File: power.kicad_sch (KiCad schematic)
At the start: 33 parts, among them J1 POWER, Q5 2N3906, Q6 2N3904, Q7 2N3904, U1 TL072, U2 TL072, U3 LM7812_TO220, U3 NE555P, U4 LM7805_TO220, U9 LM358

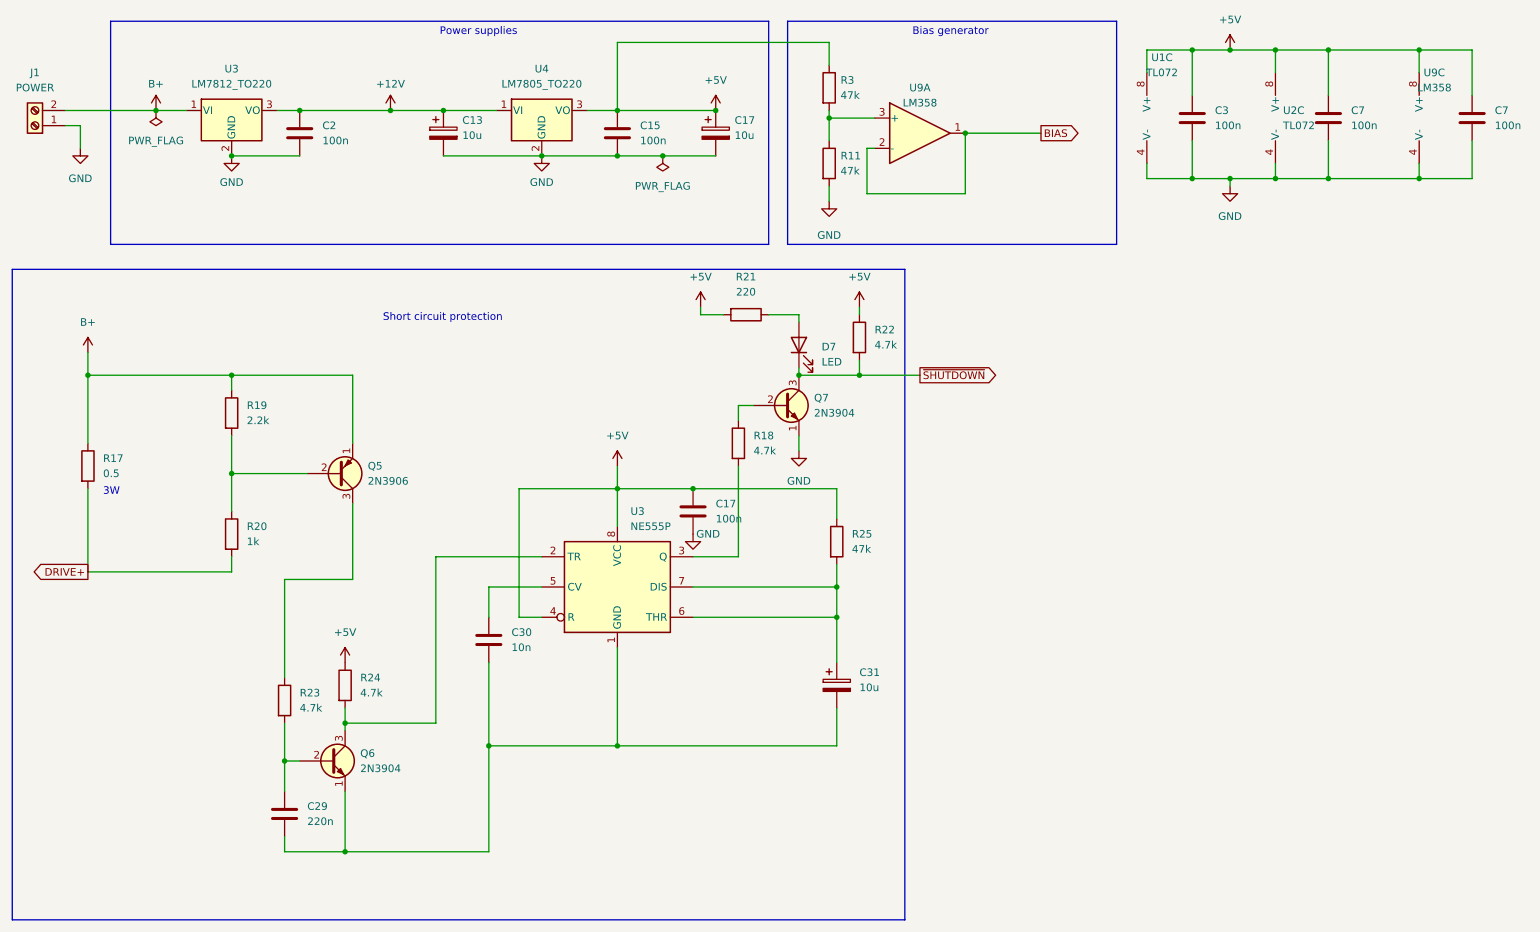
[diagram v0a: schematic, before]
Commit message: Added right channel
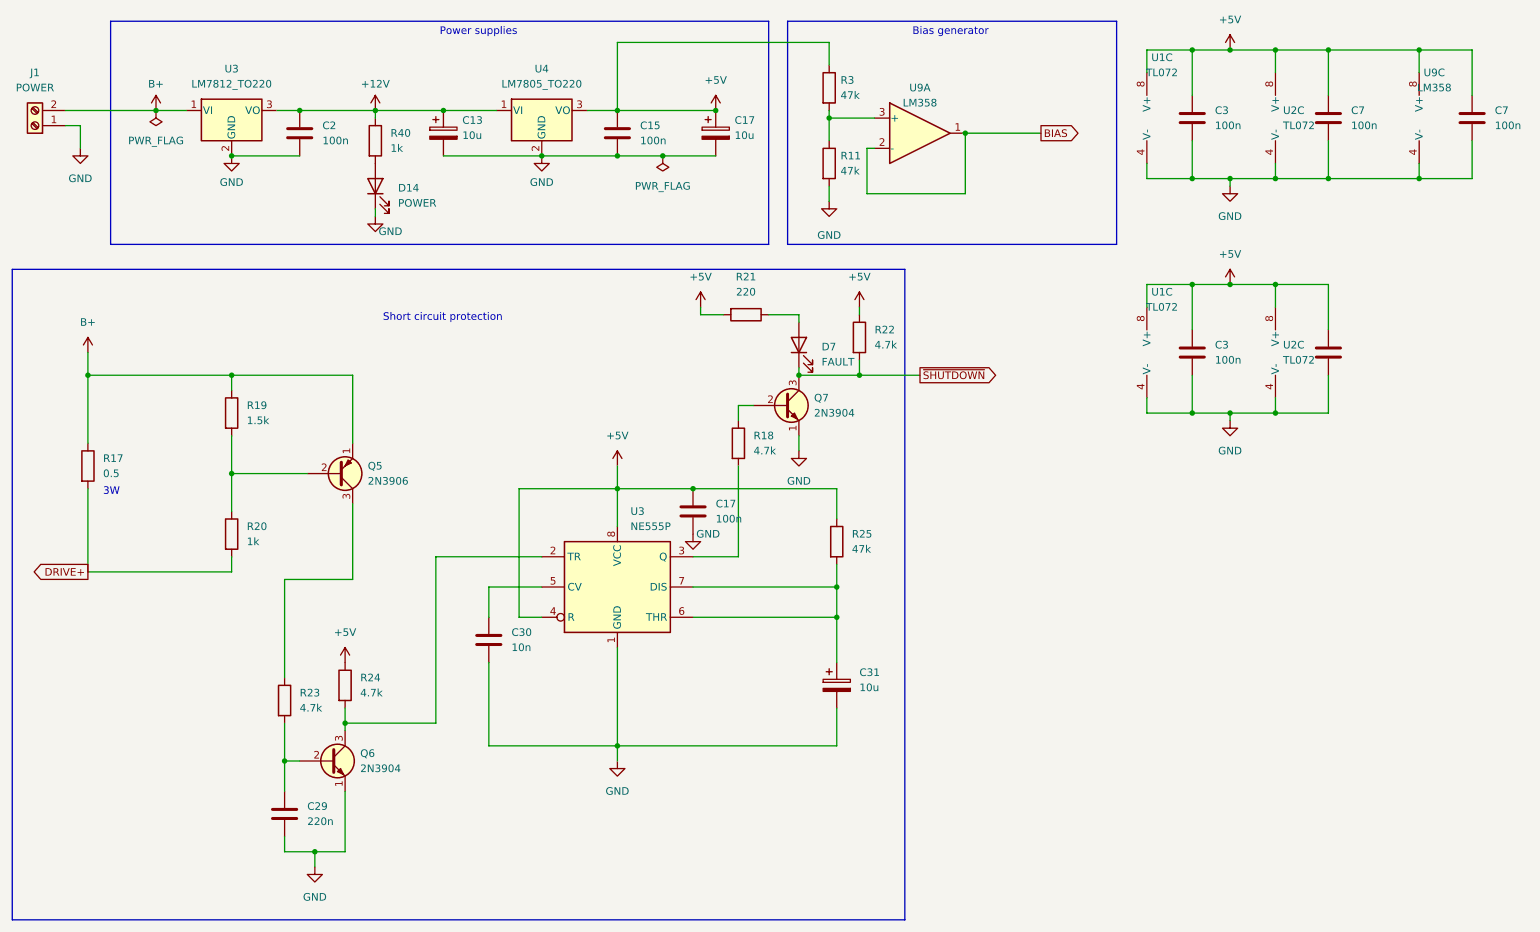
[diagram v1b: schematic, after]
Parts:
- added C3, C7: 100n, Capacitor_THT:C_Disc_D3.4mm_W2.1mm_P2.50mm, symbol Device:C
- added D14: POWER, LED_THT:LED_D4.0mm, symbol Device:LED
- added R40: 1k, Resistor_THT:R_Axial_DIN0204_L3.6mm_D1.6mm_P7.62mm_Horizontal, symbol Device:R
- added U1, U2: TL072, PCM_Package_DIP_AKL:DIP-8_W7.62mm, symbol Amplifier_Operational:TL072
- D7: value LED -> FAULT; footprint Diode_THT:D_DO-41_SOD81_P10.16mm_Horizontal -> LED_THT:LED_D4.0mm
- R19: value 2.2k -> 1.5k
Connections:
- net +12V: now also R40.1
- net +5V: now also C3.1, C7.1, U1.8 (V+), U2.8 (V+)
- net GND: now also C29.2, C30.2, C31.2, Q6.1 (E), U3.1 (GND), C3.2, C7.2, D14.1 (K), U1.4 (V-), U2.4 (V-)
- new net: D14.2 (A), R40.2

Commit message: Pre layer elimination
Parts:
- R22: value 4.7k -> 3.9k
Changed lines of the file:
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@@
       (effects (font (size 1.27 1.27)) (justify left))
     )
-    (property "Value" "4.7k" (at 170.18 81.28 0)
+    (property "Value" "3.9k" (at 170.18 81.28 0)
       (effects (font (size 1.27 1.27)) (justify left))
     )

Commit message: WIP
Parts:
- added J5: POWER, TerminalBlock_4Ucon:TerminalBlock_4Ucon_1x02_P3.50mm_Horizontal, symbol Connector:Screw_Terminal_01x02
- added Q12: 2N3906, Package_TO_SOT_THT:TO-92_Inline, symbol PCM_Transistor_BJT_AKL:2N3906
- added R43, R45: 1k, Resistor_THT:R_Axial_DIN0204_L3.6mm_D1.6mm_P7.62mm_Horizontal, symbol Device:R
- added R44: 1.5k, Resistor_THT:R_Axial_DIN0204_L3.6mm_D1.6mm_P7.62mm_Horizontal, symbol Device:R
- added R46: 4.7k, Resistor_THT:R_Axial_DIN0204_L3.6mm_D1.6mm_P7.62mm_Horizontal, symbol Device:R
- added R47: 0.5, Resistor_THT:R_Axial_DIN0922_L20.0mm_D9.0mm_P25.40mm_Horizontal, symbol Device:R
- C29: value 220n -> 10u; footprint Capacitor_THT:C_Disc_D3.4mm_W2.1mm_P2.50mm -> Capacitor_THT:CP_Radial_D4.0mm_P1.50mm; symbol Device:C -> Device:C_Polarized
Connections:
- net GND: now also J5.1 (Pin_1), R43.2
- net at C29.1, Q6.2 (B), R23.2: now also R43.1, R46.2
- net B+ renamed LPWR+
- net DRIVE+ renamed LDRIVE+
- new net: Q12.3 (C), R46.1
- new net: Q12.2 (B), R44.2, R45.1
- new net RDRIVE+: R45.2, R47.2
- new net RPWR+: J5.2 (Pin_2), Q12.1 (E), R44.1, R47.1
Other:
- moved on the sheet: Q5, Q6, R19, R20, R23, R24

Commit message: Ver 1.1
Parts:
- added unit 2 of U9
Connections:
- net GND: now also U9.5 (+)
- new net: U9.6 (-), U9.7
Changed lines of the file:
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@@
+    (stroke (width 0) (type default))
+  )
+  (wire (pts (xy 212.09 134.62) (xy 212.09 140.335))
     (stroke (width 0) (type default))
   )
@@
     (stroke (width 0) (type default))
   )
+  (wire (pts (xy 247.65 137.16) (xy 242.57 137.16))
+    (stroke (width 0) (type default))
+  )
   (wire (pts (xy 229.87 53.34) (xy 237.49 53.34))
     (stroke (width 0) (type default))
@@
     (stroke (width 0) (type default))
   )
+  (wire (pts (xy 222.885 147.32) (xy 247.65 147.32))
+    (stroke (width 0) (type default))
+  )
   (wire (pts (xy 83.82 86.36) (xy 83.82 88.9))
     (stroke (width 0) (type default))
@@
     (stroke (width 0) (type default))
   )
+  (wire (pts (xy 222.885 139.7) (xy 222.885 147.32))
+    (stroke (width 0) (type default))
+  )
   (wire (pts (xy 76.2 107.95) (xy 76.2 137.16))
     (stroke (width 0) (type default))
@@
     (stroke (width 0) (type default))
   )
+  (wire (pts (xy 227.33 134.62) (xy 212.09 134.62))
+    (stroke (width 0) (type default))
+  )
   (wire (pts (xy 223.52 71.12) (xy 229.87 71.12))
     (stroke (width 0) (type default))
@@
     (stroke (width 0) (type default))
   )
+  (wire (pts (xy 227.33 139.7) (xy 222.885 139.7))
+    (stroke (width 0) (type default))
+  )
   (wire (pts (xy 76.2 86.36) (xy 76.2 97.79))
     (stroke (width 0) (type default))
@@
   )
   (wire (pts (xy 127 148.59) (xy 163.83 148.59))
+    (stroke (width 0) (type default))
+  )
+  (wire (pts (xy 247.65 147.32) (xy 247.65 137.16))
     (stroke (width 0) (type default))
   )
@@
     (property "Intersheetrefs" "${INTERSHEET_REFS}" (at 70.07 115.57 0)
       (effects (font (size 1.27 1.27)) (justify right) hide)
+    )
+  )
+  (symbol (lib_id "power:GND") (at 212.09 140.335 0) (unit 1)
+    (in_bom yes) (on_board yes) (dnp no) (fields_autoplaced)
+    (property "Reference" "#PWR067" (at 212.09 146.685 0)
+      (effects (font (size 1.27 1.27)) hide)
+    )
+    (property "Value" "GND" (at 212.09 144.78 0)
+      (effects (font (size 1.27 1.27)))
+    )
+    (property "Footprint" "" (at 212.09 140.335 0)
+      (effects (font (size 1.27 1.27)) hide)
+    )
+    (property "Datasheet" "" (at 212.09 140.335 0)
+      (effects (font (size 1.27 1.27)) hide)
+    )
+    (pin "1")
+    (instances
+      (project "classd-amp"
+        (path "/4342a3a3-4383-4661-90ac-821979f46c8c/3b3caeaf-3878-4281-86ae-73a7190e5fd4"
+          (reference "#PWR067") (unit 1)
+        )
+      )
     )
   )
@@
         )
       )
+    )
+  )
+  (symbol (lib_id "Amplifier_Operational:LM358") (at 234.95 137.16 0) (unit 2)
+    (in_bom yes) (on_board yes) (dnp no)
+    (property "Reference" "U9" (at 234.95 129.54 0)
+      (effects (font (size 1.27 1.27)))
+    )
+    (property "Value" "LM358" (at 234.95 132.08 0)
+      (effects (font (size 1.27 1.27)))
+    )
+    (property "Footprint" "PCM_Package_DIP_AKL:DIP-8_W7.62mm" (at 234.95 137.16 0)
+      (effects (font (size 1.27 1.27)) hide)
+    )
+    (property "Datasheet" "http://www.ti.com/lit/ds/symlink/lm2904-n.pdf" (at 234.95 137.16 0)
+      (effects (font (size 1.27 1.27)) hide)
+    )
+    (property "Sim.Library" "lm358.txt" (at 234.95 121.92 0)
+      (effects (font (size 1.27 1.27)) hide)
+    )
+    (property "Sim.Name" "LM358" (at 234.95 124.46 0)
+      (effects (font (size 1.27 1.27)) hide)
+    )
+    (property "Sim.Device" "SUBCKT" (at 234.95 127 0)
+      (effects (font (size 1.27 1.27)) hide)
+    )
+    (property "Sim.Pins" "2=1 3=2 4=5 8=4" (at 234.95 129.54 0)
+      (effects (font (size 1.27 1.27)) hide)
+    )
+    (pin "1")
+    (pin "2")
+    (pin "3")
+    (pin "5")
+    (pin "6")
+    (pin "7")
+    (pin "4")
+    (pin "8")
+    (instances
+      (project "classd-amp"
+        (path "/4342a3a3-4383-4661-90ac-821979f46c8c/3b3caeaf-3878-4281-86ae-73a7190e5fd4"
+          (reference "U9") (unit 2)
+        )
+      )

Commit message: WIP
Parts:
- renumbered C2 to C25, C13 to C26, C15 to C27, C17 to C28, C7 to C32, C3 to C48, C7 to C49, R3 to R15, R11 to R16, U1 to U10, U2 to U11, U3 to U7, U4 to U8

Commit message: WIP
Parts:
- U1, U10, U11, U2, U9: footprint PCM_Package_DIP_AKL:DIP-8_W7.62mm -> Package_DIP:DIP-8_W7.62mm
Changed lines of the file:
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@@
 			)
 		)
-		(property "Footprint" "PCM_Package_DIP_AKL:DIP-8_W7.62mm"
+		(property "Footprint" "Package_DIP:DIP-8_W7.62mm"
 			(at 240.03 43.18 0)
 			(effects
@@
 			)
 		)
-		(property "Footprint" "PCM_Package_DIP_AKL:DIP-8_W7.62mm"
+		(property "Footprint" "Package_DIP:DIP-8_W7.62mm"
 			(at 234.95 137.16 0)
 			(effects
@@
 			)
 		)
-		(property "Footprint" "PCM_Package_DIP_AKL:DIP-8_W7.62mm"
+		(property "Footprint" "Package_DIP:DIP-8_W7.62mm"
 			(at 218.44 82.55 0)
 			(effects
@@
 			)
 		)
-		(property "Footprint" "PCM_Package_DIP_AKL:DIP-8_W7.62mm"
+		(property "Footprint" "Package_DIP:DIP-8_W7.62mm"
 			(at 240.03 82.55 0)
 			(effects
@@
 			)
 		)
-		(property "Footprint" "PCM_Package_DIP_AKL:DIP-8_W7.62mm"
+		(property "Footprint" "Package_DIP:DIP-8_W7.62mm"
 			(at 264.16 43.18 0)
 			(effects
@@
 			)
 		)
-		(property "Footprint" "PCM_Package_DIP_AKL:DIP-8_W7.62mm"
+		(property "Footprint" "Package_DIP:DIP-8_W7.62mm"
 			(at 177.8 45.72 0)
 			(effects
@@
 			)
 		)
-		(property "Footprint" "PCM_Package_DIP_AKL:DIP-8_W7.62mm"
+		(property "Footprint" "Package_DIP:DIP-8_W7.62mm"
 			(at 218.44 43.18 0)
 			(effects
